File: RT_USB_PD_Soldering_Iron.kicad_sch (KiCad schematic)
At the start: 58 parts, among them J1 USB4105-GF-A, J2 35RASMT4BHNTRX, J3 Conn_02x03_Odd_Even, SW1 SW_Push, SW2 SW_Push, U1 SPX3819M5-L-3-3, U2 BMI270, U3 DRTR5V0U4S-7, U5 STM32G431Kxxx, U6 TPS25982ONRGET, U7 OPA376AIDCKR, U8 STTS22H, Y1 NX2016SA-24MHZ-EXS00A-CS10820

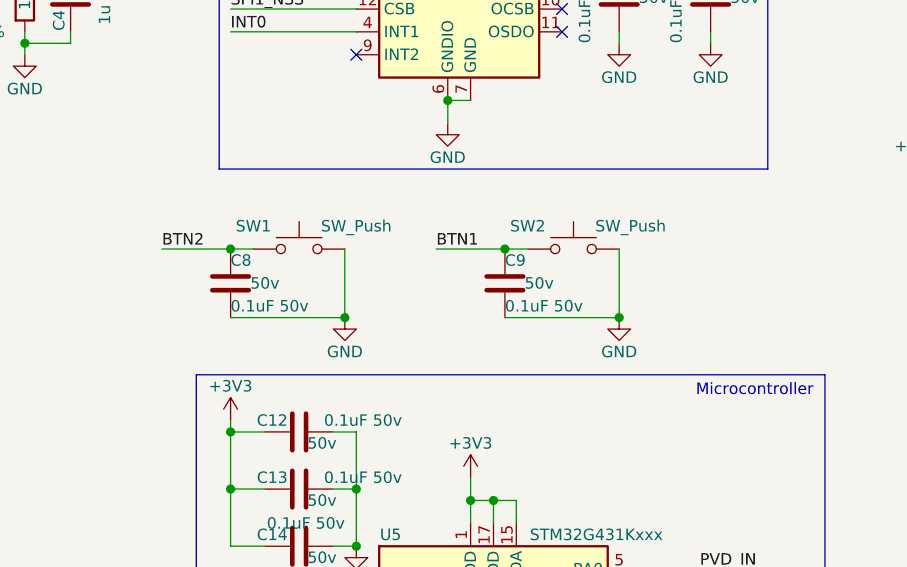
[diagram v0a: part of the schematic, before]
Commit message: Update buttons to use active-high
by using active high, button1 allows boot mode selection when pressed.
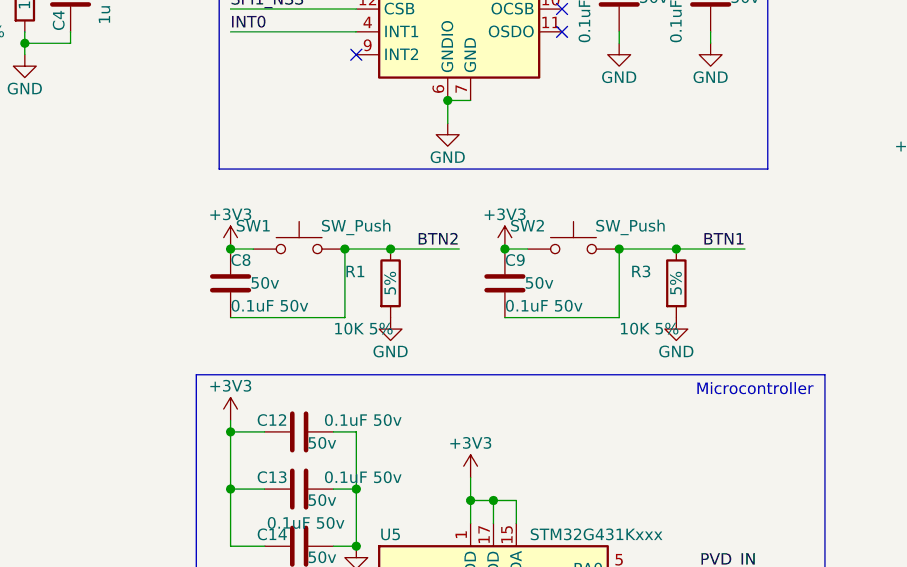
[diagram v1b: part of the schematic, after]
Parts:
- added R1, R3: 10K 5%, Resistor_SMD:R_0402_1005Metric, symbol Device:R
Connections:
- net +3V3: now also C8.1, C9.1, SW1.1, SW2.1
- net BTN1: now also C9.2, SW2.2, R3.1; no longer C9.1, SW2.1
- net BTN2: now also C8.2, SW1.2, R1.1; no longer C8.1, SW1.1
- net GND: now also R1.2, R3.2; no longer C8.2, C9.2, SW1.2, SW2.2
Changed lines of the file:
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@@
   (junction (at 152.4 91.44) (diameter 1.016) (color 0 0 0 0))
   (junction (at 152.4 97.79) (diameter 1.016) (color 0 0 0 0))
-  (junction (at 165.1 78.74) (diameter 1.016) (color 0 0 0 0))
+  (junction (at 165.1 71.12) (diameter 1.016) (color 0 0 0 0))
   (junction (at 166.37 97.79) (diameter 1.016) (color 0 0 0 0))
   (junction (at 166.37 104.14) (diameter 1.016) (color 0 0 0 0))
+  (junction (at 170.18 71.12) (diameter 1.016) (color 0 0 0 0))
   (junction (at 176.53 31.75) (diameter 1.016) (color 0 0 0 0))
   (junction (at 176.53 54.61) (diameter 1.016) (color 0 0 0 0))
@@
   (junction (at 181.61 149.86) (diameter 1.016) (color 0 0 0 0))
   (junction (at 182.88 71.12) (diameter 1.016) (color 0 0 0 0))
-  (junction (at 195.58 78.74) (diameter 1.016) (color 0 0 0 0))
+  (junction (at 195.58 71.12) (diameter 1.016) (color 0 0 0 0))
+  (junction (at 201.93 71.12) (diameter 1.016) (color 0 0 0 0))
   (junction (at 210.82 129.54) (diameter 1.016) (color 0 0 0 0))
   (junction (at 232.41 149.86) (diameter 1.016) (color 0 0 0 0))
@@
     (stroke (width 0) (type solid) (color 0 0 0 0))
   )
-  (wire (pts (xy 144.78 71.12) (xy 152.4 71.12))
-    (stroke (width 0) (type solid) (color 0 0 0 0))
-  )
   (wire (pts (xy 151.13 170.18) (xy 151.13 171.45))
     (stroke (width 0) (type solid) (color 0 0 0 0))
@@
     (stroke (width 0) (type solid) (color 0 0 0 0))
   )
+  (wire (pts (xy 165.1 71.12) (xy 170.18 71.12))
+    (stroke (width 0) (type solid) (color 0 0 0 0))
+  )
   (wire (pts (xy 166.37 91.44) (xy 166.37 97.79))
     (stroke (width 0) (type solid) (color 0 0 0 0))
@@
     (stroke (width 0) (type solid) (color 0 0 0 0))
   )
-  (wire (pts (xy 175.26 71.12) (xy 182.88 71.12))
+  (wire (pts (xy 170.18 71.12) (xy 177.8 71.12))
     (stroke (width 0) (type solid) (color 0 0 0 0))
   )
@@
     (stroke (width 0) (type solid) (color 0 0 0 0))
   )
+  (wire (pts (xy 195.58 71.12) (xy 201.93 71.12))
+    (stroke (width 0) (type solid) (color 0 0 0 0))
+  )
   (wire (pts (xy 196.85 106.68) (xy 210.82 106.68))
     (stroke (width 0) (type solid) (color 0 0 0 0))
@@
   )
   (wire (pts (xy 196.85 144.78) (xy 210.82 144.78))
+    (stroke (width 0) (type solid) (color 0 0 0 0))
+  )
+  (wire (pts (xy 201.93 71.12) (xy 209.55 71.12))
     (stroke (width 0) (type solid) (color 0 0 0 0))
   )
@@
     (effects (font (size 1.27 1.27)) (justify right bottom))
   )
-  (label "BTN2" (at 144.78 71.12 0)
-    (effects (font (size 1.27 1.27)) (justify left bottom))
-  )
   (label "SPI1_MISO" (at 152.4 36.83 0)
     (effects (font (size 1.27 1.27)) (justify left bottom))
@@
     (effects (font (size 1.27 1.27)) (justify left bottom))
   )
-  (label "BTN1" (at 175.26 71.12 0)
-    (effects (font (size 1.27 1.27)) (justify left bottom))
+  (label "BTN2" (at 177.8 71.12 180)
+    (effects (font (size 1.27 1.27)) (justify right bottom))
+  )
+  (label "BTN1" (at 209.55 71.12 180)
+    (effects (font (size 1.27 1.27)) (justify right bottom))
   )
   (label "PVD_IN" (at 210.82 106.68 180)
@@
     )
   )
+  (symbol (lib_id "power:+3V3") (at 152.4 71.12 0) (unit 1)
+    (in_bom yes) (on_board yes)
+    (property "Reference" "#PWR05" (id 0) (at 152.4 74.93 0)
+      (effects (font (size 1.27 1.27)) hide)
+    )
+    (property "Value" "+3V3" (id 1) (at 152.4 67.31 0))
+    (property "Footprint" "" (id 2) (at 152.4 71.12 0)
+      (effects (font (size 1.27 1.27)) hide)
+    )
+    (property "Datasheet" "" (id 3) (at 152.4 71.12 0)
+      (effects (font (size 1.27 1.27)) hide)
+    )
+  )
   (symbol (lib_id "power:+3V3") (at 152.4 90.17 0) (unit 1)
     (in_bom yes) (on_board yes)
@@
     )
   )
+  (symbol (lib_id "power:+3V3") (at 182.88 71.12 0) (unit 1)
+    (in_bom yes) (on_board yes)
+    (property "Reference" "#PWR06" (id 0) (at 182.88 74.93 0)
+      (effects (font (size 1.27 1.27)) hide)
+    )
+    (property "Value" "+3V3" (id 1) (at 182.88 67.31 0))
+    (property "Footprint" "" (id 2) (at 182.88 71.12 0)
+      (effects (font (size 1.27 1.27)) hide)
+    )
+    (property "Datasheet" "" (id 3) (at 182.88 71.12 0)
+      (effects (font (size 1.27 1.27)) hide)
+    )
+  )
   (symbol (lib_id "power:+3V3") (at 195.58 38.1 0) (unit 1)
     (in_bom yes) (on_board yes)
@@
     )
   )
-  (symbol (lib_id "power:GND") (at 165.1 78.74 0) (unit 1)
-    (in_bom yes) (on_board yes)
-    (property "Reference" "#PWR0141" (id 0) (at 165.1 85.09 0)
-      (effects (font (size 1.27 1.27)) hide)
-    )
-    (property "Value" "GND" (id 1) (at 165.1 82.55 0))
-    (property "Footprint" "" (id 2) (at 165.1 78.74 0)
-      (effects (font (size 1.27 1.27)) hide)
-    )
-    (property "Datasheet" "" (id 3) (at 165.1 78.74 0)
-      (effects (font (size 1.27 1.27)) hide)
-    )
-  )
   (symbol (lib_id "power:GND") (at 166.37 104.14 0) (unit 1)
     (in_bom yes) (on_board yes)
@@
     )
   )
+  (symbol (lib_id "power:GND") (at 170.18 78.74 0) (unit 1)
+    (in_bom yes) (on_board yes)
+    (property "Reference" "#PWR0141" (id 0) (at 170.18 85.09 0)
+      (effects (font (size 1.27 1.27)) hide)
+    )
+    (property "Value" "GND" (id 1) (at 170.18 82.55 0))
+    (property "Footprint" "" (id 2) (at 170.18 78.74 0)
+      (effects (font (size 1.27 1.27)) hide)
+    )
+    (property "Datasheet" "" (id 3) (at 170.18 78.74 0)
+      (effects (font (size 1.27 1.27)) hide)
+    )
+  )
   (symbol (lib_id "power:GND") (at 176.53 57.15 0) (unit 1)
     (in_bom yes) (on_board yes)
@@
     )
   )
-  (symbol (lib_id "power:GND") (at 195.58 78.74 0) (unit 1)
-    (in_bom yes) (on_board yes)
-    (property "Reference" "#PWR0142" (id 0) (at 195.58 85.09 0)
-      (effects (font (size 1.27 1.27)) hide)
-    )
-    (property "Value" "GND" (id 1) (at 195.58 82.55 0))
-    (property "Footprint" "" (id 2) (at 195.58 78.74 0)
-      (effects (font (size 1.27 1.27)) hide)
-    )
-    (property "Datasheet" "" (id 3) (at 195.58 78.74 0)
+  (symbol (lib_id "power:GND") (at 201.93 78.74 0) (unit 1)
+    (in_bom yes) (on_board yes)
+    (property "Reference" "#PWR0142" (id 0) (at 201.93 85.09 0)
+      (effects (font (size 1.27 1.27)) hide)
+    )
+    (property "Value" "GND" (id 1) (at 201.93 82.55 0))
+    (property "Footprint" "" (id 2) (at 201.93 78.74 0)
+      (effects (font (size 1.27 1.27)) hide)
+    )
+    (property "Datasheet" "" (id 3) (at 201.93 78.74 0)
       (effects (font (size 1.27 1.27)) hide)
     )
@@
     )
     (property "Tolerance" "1%" (id 4) (at 129.54 43.18 90))
+  )
+  (symbol (lib_id "Device:R") (at 170.18 74.93 0) (unit 1)
+    (in_bom yes) (on_board yes)
+    (property "Reference" "R1" (id 0) (at 165.1 73.66 0)
+      (effects (font (size 1.27 1.27)) (justify left))
+    )
+    (property "Value" "10K 5%" (id 1) (at 163.83 80.01 0)
+      (effects (font (size 1.27 1.27)) (justify left))
+    )
+    (property "Footprint" "Resistor_SMD:R_0402_1005Metric" (id 2) (at 168.402 74.93 90)
+      (effects (font (size 1.27 1.27)) hide)
+    )
+    (property "Datasheet" "~" (id 3) (at 170.18 74.93 0)
+      (effects (font (size 1.27 1.27)) hide)
+    )
+    (property "Tolerance" "5%" (id 4) (at 170.18 74.93 90))
+  )
+  (symbol (lib_id "Device:R") (at 201.93 74.93 0) (unit 1)
+    (in_bom yes) (on_board yes)
+    (property "Reference" "R3" (id 0) (at 196.85 73.66 0)
+      (effects (font (size 1.27 1.27)) (justify left))
+    )
+    (property "Value" "10K 5%" (id 1) (at 195.58 80.01 0)
+      (effects (font (size 1.27 1.27)) (justify left))
+    )
+    (property "Footprint" "Resistor_SMD:R_0402_1005Metric" (id 2) (at 200.152 74.93 90)
+      (effects (font (size 1.27 1.27)) hide)
+    )
+    (property "Datasheet" "~" (id 3) (at 201.93 74.93 0)
+      (effects (font (size 1.27 1.27)) hide)
+    )
+    (property "Tolerance" "5%" (id 4) (at 201.93 74.93 90))
   )
   (symbol (lib_id "Device:R") (at 247.65 149.86 90) (unit 1)
@@
       (reference "#PWR04") (unit 1) (value "GND") (footprint "")
     )
+    (path "/dc471647-d1de-4cfa-a24f-56c525f83477"
+      (reference "#PWR05") (unit 1) (value "+3V3") (footprint "")
+    )
+    (path "/21881027-bbf0-448a-bcd4-fcb73ae0705d"
+      (reference "#PWR06") (unit 1) (value "+3V3") (footprint "")
+    )
     (path "/3b1283f9-2394-4e24-a894-33262dc732f7"
       (reference "#PWR0101") (unit 1) (value "+3V3") (footprint "")
@@
       (reference "OLED1") (unit 1) (value "ER-OLED0.87") (footprint "ER-OLED0.87:ER-OLED0.87")
     )
+    (path "/a7f7da36-ce34-4333-af45-c2037e2f5e6c"
+      (reference "R1") (unit 1) (value "10K 5%") (footprint "Resistor_SMD:R_0402_1005Metric")
+    )
     (path "/88027881-d3dc-4c8f-8a89-19c23e8fc164"
       (reference "R2") (unit 1) (value "120K 1%") (footprint "Resistor_SMD:R_0402_1005Metric")
     )
+    (path "/386f87b9-aa30-4751-b961-5fc9e2b92331"
+      (reference "R3") (unit 1) (value "10K 5%") (footprint "Resistor_SMD:R_0402_1005Metric")
+    )
     (path "/1a2c38a0-0095-470b-8400-3a8bdde888af"

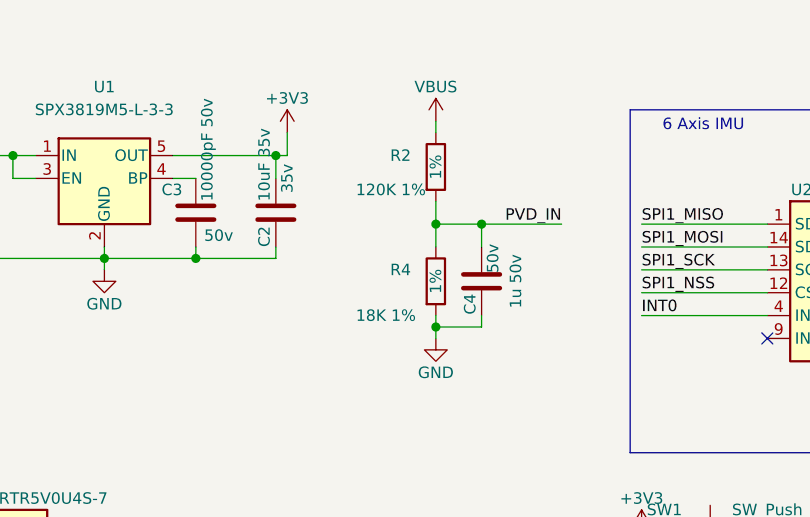
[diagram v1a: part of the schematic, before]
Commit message: Update Power voltage circuit to higher precision and lower cost components
change to 12K + 75K 0.5%
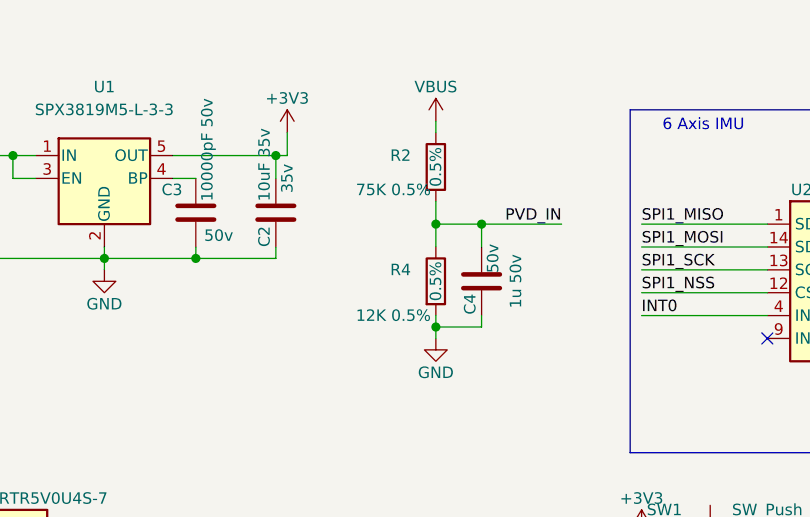
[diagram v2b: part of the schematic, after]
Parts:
- R2: value 120K 1% -> 75K 0.5%; Tolerance 1% -> 0.5%
- R4: value 18K 1% -> 12K 0.5%; Tolerance 1% -> 0.5%
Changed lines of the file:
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@@
   (junction (at 232.41 154.94) (diameter 1.016) (color 0 0 0 0))
   (junction (at 243.84 132.08) (diameter 1.016) (color 0 0 0 0))
-  (no_connect (at 43.18 50.8))
   (no_connect (at 147.32 176.53))
   (no_connect (at 189.23 44.45))
+  (no_connect (at 43.18 50.8))
+  (no_connect (at 189.23 46.99))
   (no_connect (at 189.23 41.91))
+  (no_connect (at 166.37 49.53))
+  (no_connect (at 43.18 53.34))
   (no_connect (at 189.23 39.37))
-  (no_connect (at 43.18 53.34))
-  (no_connect (at 189.23 46.99))
-  (no_connect (at 166.37 49.53))
   (wire (pts (xy 17.78 168.91) (xy 29.21 168.91))
     (stroke (width 0) (type solid) (color 0 0 0 0))
@@
       (effects (font (size 1.27 1.27)) (justify left))
     )
-    (property "Value" "120K 1%" (id 1) (at 120.65 33.02 0)
+    (property "Value" "75K 0.5%" (id 1) (at 120.65 33.02 0)
       (effects (font (size 1.27 1.27)) (justify left))
     )
@@
       (effects (font (size 1.27 1.27)) hide)
     )
-    (property "Tolerance" "1%" (id 4) (at 129.54 30.48 90))
+    (property "Tolerance" "0.5%" (id 4) (at 129.54 30.48 90))
   )
   (symbol (lib_id "Device:R") (at 129.54 43.18 0) (unit 1)
@@
       (effects (font (size 1.27 1.27)) (justify left))
     )
-    (property "Value" "18K 1%" (id 1) (at 120.65 46.99 0)
+    (property "Value" "12K 0.5%" (id 1) (at 120.65 46.99 0)
       (effects (font (size 1.27 1.27)) (justify left))
     )
@@
       (effects (font (size 1.27 1.27)) hide)
     )
-    (property "Tolerance" "1%" (id 4) (at 129.54 43.18 90))
+    (property "Tolerance" "0.5%" (id 4) (at 129.54 43.18 90))
   )
   (symbol (lib_id "Device:R") (at 170.18 74.93 0) (unit 1)
@@
     )
     (path "/88027881-d3dc-4c8f-8a89-19c23e8fc164"
-      (reference "R2") (unit 1) (value "120K 1%") (footprint "Resistor_SMD:R_0402_1005Metric")
+      (reference "R2") (unit 1) (value "75K 0.5%") (footprint "Resistor_SMD:R_0402_1005Metric")
     )
     (path "/386f87b9-aa30-4751-b961-5fc9e2b92331"
@@
     )
     (path "/1a2c38a0-0095-470b-8400-3a8bdde888af"
-      (reference "R4") (unit 1) (value "18K 1%") (footprint "Resistor_SMD:R_0402_1005Metric")
+      (reference "R4") (unit 1) (value "12K 0.5%") (footprint "Resistor_SMD:R_0402_1005Metric")
     )
     (path "/8fec0000-de8e-4e27-8a43-083d5fd52b1a"

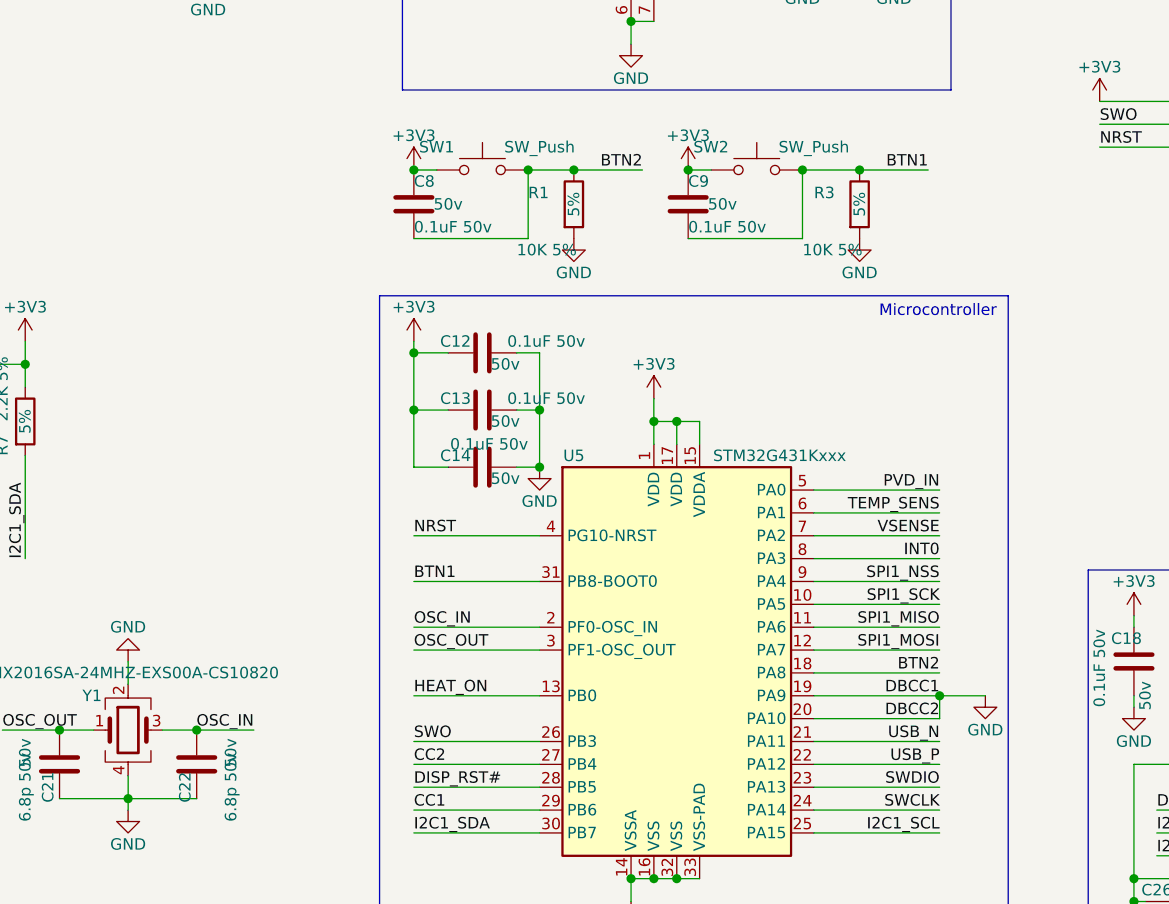
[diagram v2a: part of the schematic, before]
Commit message: Modify CC lines
Add capacitors to CC lines. Tie in DBCC to the CC lines.
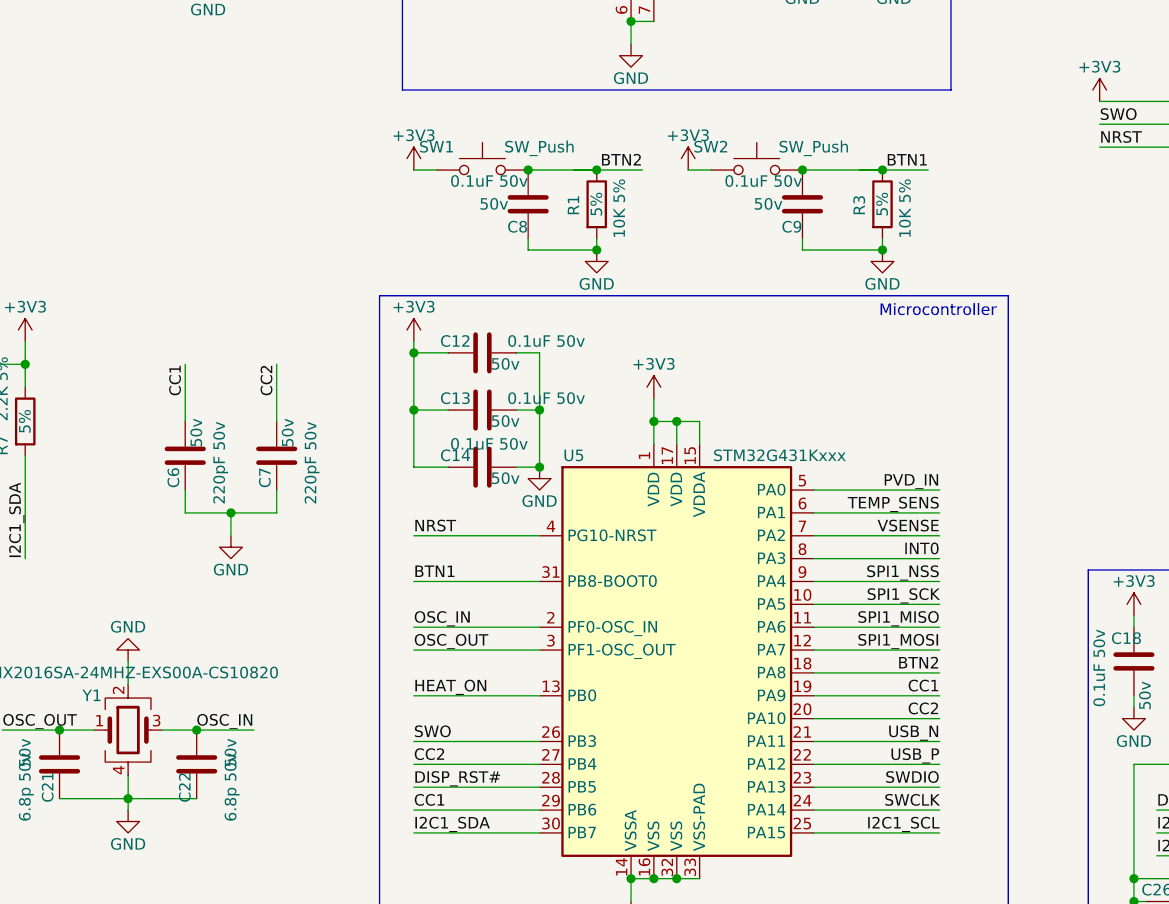
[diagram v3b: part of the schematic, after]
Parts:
- added C6, C7: 220pF 50v, Capacitor_SMD:C_0402_1005Metric, symbol Device:C
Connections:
- net +3V3: no longer C8.1, C9.1
- net CC1: now also U5.19 (PA9), C6.2
- net CC2: now also U5.20 (PA10), C7.2
- net GND: now also C8.1, C9.1, C6.1, C7.1; no longer U5.19 (PA9), U5.20 (PA10)
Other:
- moved on the sheet: C8, C9, R1, R3

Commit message: First revision 0.1
Rev 0.1 untested unverified.
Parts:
- removed C21, C22: 6.8p 50v, Capacitor_SMD:C_0402_1005Metric, symbol Device:C
- removed C29: 0.1uF 50v, Capacitor_SMD:C_0402_1005Metric, symbol Device:C
- removed U3: DRTR5V0U4S-7, Package_TO_SOT_SMD:SOT-363_SC-70-6, symbol Power_Protection:USBLC6-4SC6
- removed U8: STTS22H, Package_DFN_QFN:DFN-6-1EP_2x2mm_P0.65mm_EP1x1.6mm, symbol STTS22HTR:STTS22H
- removed Y1: NX2016SA-24MHZ-EXS00A-CS10820, Crystal:Crystal_SMD_2016-4Pin_2.0x1.6mm, symbol Device:Crystal_GND24
- added C? (x2): 220pF 50v, Capacitor_SMD:C_0402_1005Metric, symbol Device:C
- added TH1: Thermistor_NTC, Resistor_SMD:R_0402_1005Metric, symbol Device:Thermistor_NTC
- added U3: ECMF02-AMX6, Package_DFN_QFN:ST_UQFN-6L_1.5x1.7mm_Pitch0.5mm, symbol ECMF02-AMX6:ECMF02-AMX6
- added U4: FUSB302BMPX, Package_DFN_QFN:WQFN-14-1EP_2.5x2.5mm_P0.5mm_EP1.45x1.45mm, symbol Interface_USB:FUSB302BMPX
- C4: value 1u 50v -> 10uF 35v; footprint Capacitor_SMD:C_0402_1005Metric -> Capacitor_SMD:C_0603_1608Metric_Pad1.05x0.95mm_HandSolder; Voltage 50v -> 35v
- C6: value 220pF 50v -> 1u 50v
- C7: value 220pF 50v -> 0.1uF 50v
- R2: value 75K 0.5% -> 10K 1%; Tolerance 0.5% -> 1%
- R4: value 12K 0.5% -> 2.2K 5%; Tolerance 0.5% -> 5%
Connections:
- net +3V3: now also C7.2, R2.1, R4.1, U4.3 (VDD), U4.4 (VDD)
- net CC1: now also C?.2, U4.10 (CC1), U4.11 (CC1); no longer C6.2, U5.19 (PA9), U5.29 (PB6)
- net CC2: now also C?.2, U4.1 (CC2), U4.14 (CC2); no longer C7.2, U5.20 (PA10), U5.27 (PB4)
- net GND: now also C4.2, C?.1, C?.1, TH1.2, U3.3 (GND), U3.4 (NC), U4.15 (GND), U4.8 (GND), U4.9 (GND); no longer C4.1, R4.2
- net I2C1_SCL: now also U4.6 (SCL)
- net I2C1_SDA: now also U4.7 (SDA)
- net IN: now also C4.1, U4.2 (VBUS); no longer R2.1
- net USB_N: now also U3.6; no longer J1.A7 (D-), J1.B7 (D-)
- net USB_P: now also U3.5; no longer J1.A6 (D+), J1.B6 (D+)
- net INT0 renamed BMI270_INT0
- net OSC_IN: no longer names the net of U5.2 (PF0-OSC_IN)
- net OSC_OUT: no longer names the net of U5.3 (PF1-OSC_OUT)
- net PVD_IN renamed BOARD_TEMP
- net BOARD_TEMP: now also C6.2, TH1.1; no longer C4.2, R4.1
- new net FUSB_INT_N: R4.2, U4.5 (INT_N), U5.19 (PA9)
- new net USB_N_IN: J1.A7 (D-), J1.B7 (D-), U3.1
- new net USB_P_IN: J1.A6 (D+), J1.B6 (D+), U3.2
- no-connect marks 8 -> 7
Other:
- moved on the sheet: C1, C15, D2, J2
